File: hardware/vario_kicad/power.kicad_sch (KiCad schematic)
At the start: 17 parts, among them Q1 NMOS, Q2 PMOS

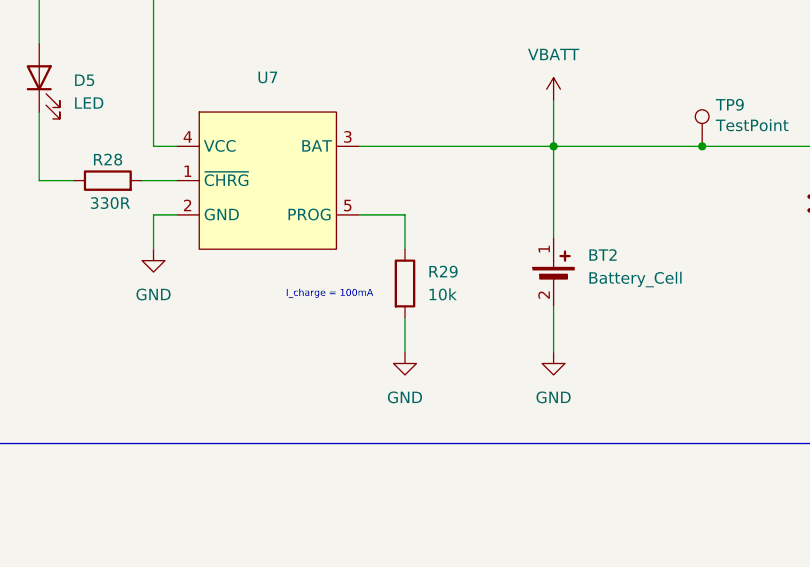
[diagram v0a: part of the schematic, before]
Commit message: update footprints, add LSE oscillator
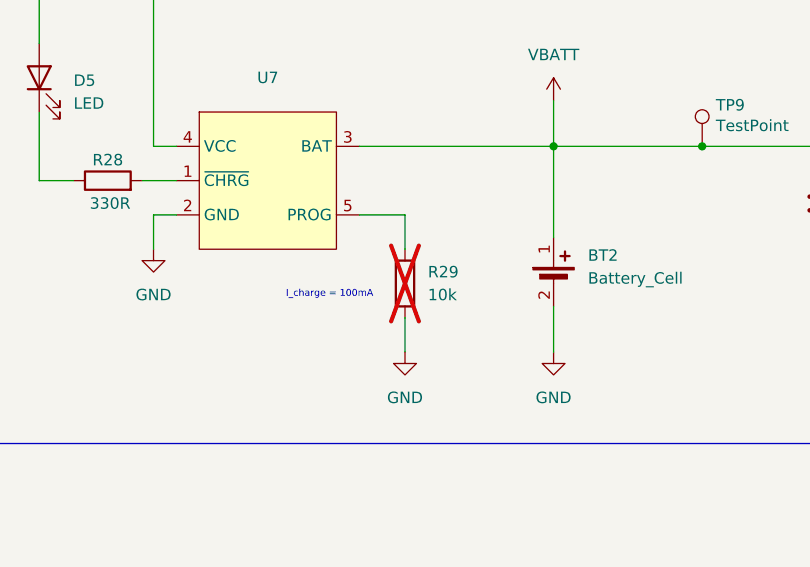
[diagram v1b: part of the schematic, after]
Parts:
- R22, R23, R24, R25, R28: footprint (none) -> Resistor_SMD:R_0402_1005Metric
- R29: footprint (none) -> Resistor_SMD:R_0402_1005Metric; now not fitted
- TP10, TP9: footprint (none) -> TestPoint:TestPoint_Pad_D1.0mm
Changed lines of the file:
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@@
 			)
 		)
-		(property "Footprint" ""
+		(property "Footprint" "Resistor_SMD:R_0402_1005Metric"
 			(at 54.102 158.75 90)
 			(effects
@@
 			)
 		)
-		(property "Footprint" ""
+		(property "Footprint" "Resistor_SMD:R_0402_1005Metric"
 			(at 80.772 146.05 90)
 			(effects
@@
 			)
 		)
-		(property "Footprint" ""
+		(property "Footprint" "Resistor_SMD:R_0402_1005Metric"
 			(at 80.772 161.29 90)
 			(effects
@@
 			)
 		)
-		(property "Footprint" ""
+		(property "Footprint" "Resistor_SMD:R_0402_1005Metric"
 			(at 57.15 58.928 90)
 			(effects
@@
 			)
 		)
-		(property "Footprint" ""
+		(property "Footprint" "TestPoint:TestPoint_Pad_D1.0mm"
 			(at 196.85 53.34 0)
 			(effects
@@
 			)
 		)
-		(property "Footprint" ""
+		(property "Footprint" "Resistor_SMD:R_0402_1005Metric"
 			(at 54.61 127.508 90)
 			(effects
@@
 			)
 		)
-		(property "Footprint" ""
+		(property "Footprint" "TestPoint:TestPoint_Pad_D1.0mm"
 			(at 128.27 53.34 0)
 			(effects
@@
 		(in_bom yes)
 		(on_board yes)
-		(dnp no)
+		(dnp yes)
 		(fields_autoplaced yes)
 		(property "Reference" "R29"
@@
 			)
 		)
-		(property "Footprint" ""
+		(property "Footprint" "Resistor_SMD:R_0402_1005Metric"
 			(at 88.392 68.58 90)
 			(effects

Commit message: start layout
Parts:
- added P1: USB_C_Plug_USB2.0, symbol_lib:my_usbc, symbol Connector:USB_C_Plug_USB2.0
- added R4: 5k1, Resistor_SMD:R_0402_1005Metric, symbol Device:R
- Q1, Q2: footprint (none) -> Package_TO_SOT_SMD:SOT-23_Handsoldering
- R29: now fitted
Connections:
- net GND: now also Q1.2 (S), P1.A1 (GND), P1.A12 (GND), P1.B1 (GND), P1.B12 (GND), P1.S1 (SHIELD), R4.1; no longer Q1.3 (S)
- net VBATT: now also Q2.2 (S), U8.3 (VIN); no longer Q2.3 (S), U8.2 (VOUT)
- net VBATT_SW: now also Q2.3 (D); no longer Q2.1 (D)
- net V_BATT_SW_EN: now also Q1.1 (G); no longer Q1.2 (G)
- net V_USB: now also P1.A4 (VBUS), P1.A9 (VBUS), P1.B4 (VBUS), P1.B9 (VBUS)
- new net: P1.A5 (CC), R4.2
- new net: Q1.3 (D), Q2.1 (G), R22.1
- new net USB_D+: P1.A6 (D+)
- new net USB_D-: P1.A7 (D-)
- no-connect marks 0 -> 1
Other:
- moved on the sheet: BT2, C14, C18, C19, D5, R28, TP10, TP9, U7, U8

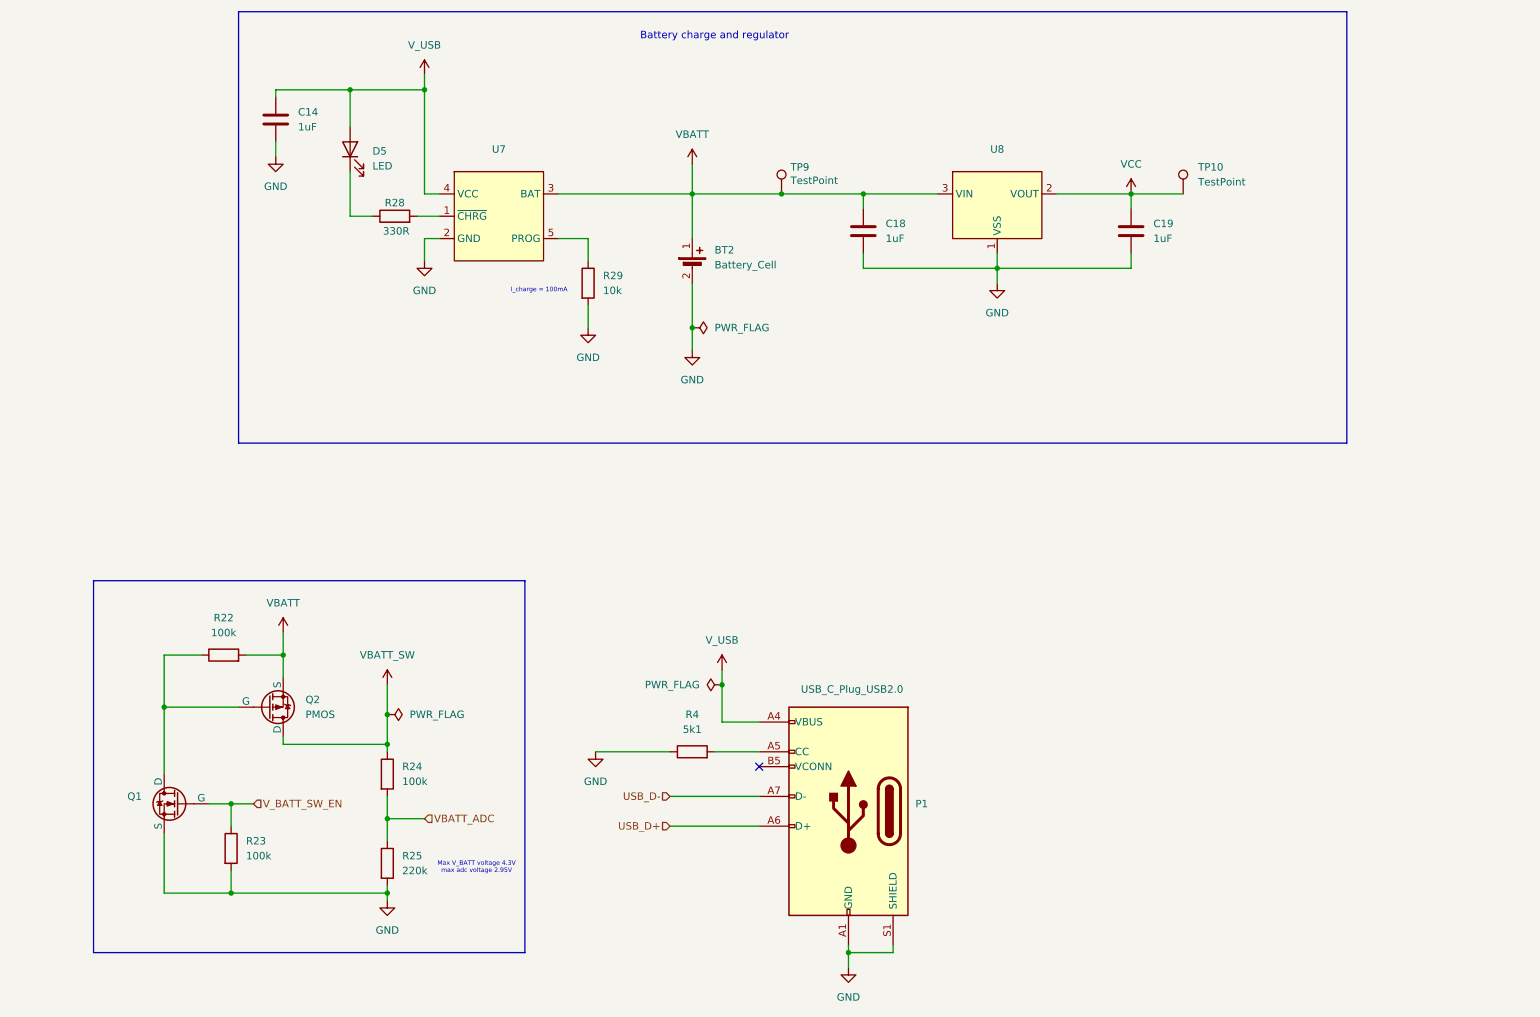
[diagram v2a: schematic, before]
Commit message: update usb c, minor other updates
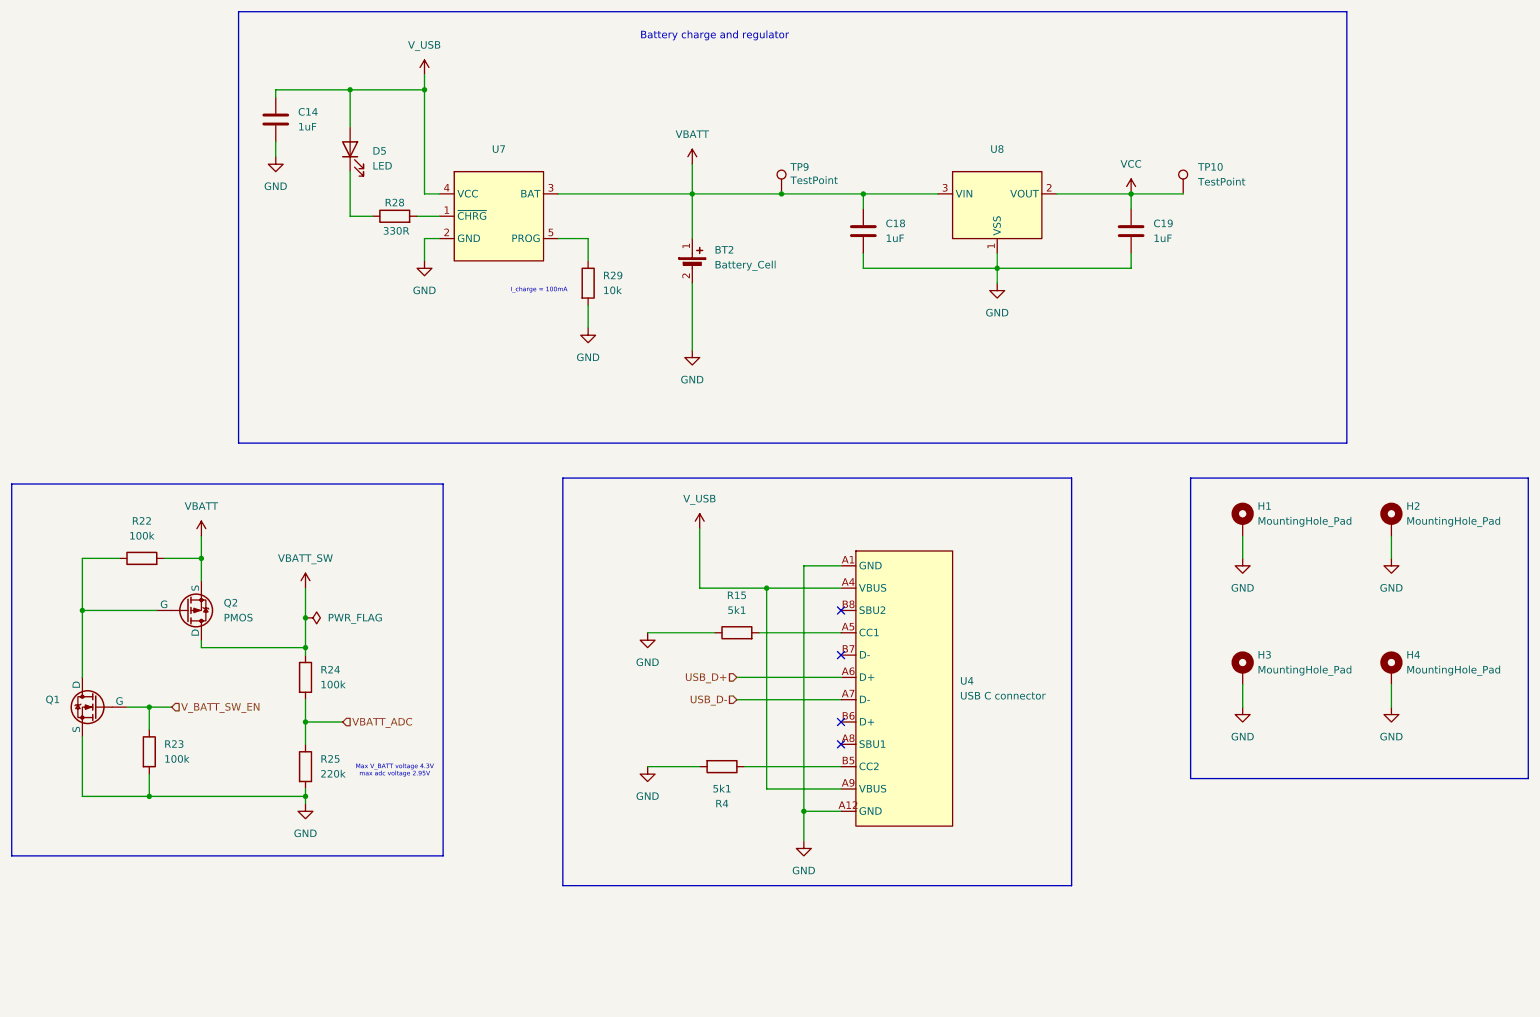
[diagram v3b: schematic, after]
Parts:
- removed P1: USB_C_Plug_USB2.0, symbol_lib:my_usbc, symbol Connector:USB_C_Plug_USB2.0
- added H1, H2, H3, H4: MountingHole_Pad, MountingHole:MountingHole_2.2mm_M2_ISO7380_Pad, symbol Mechanical:MountingHole_Pad
- added R15: 5k1, Resistor_SMD:R_0402_1005Metric, symbol Device:R
- added U4: USB C connector, symbol_lib:my_usbc, symbol New_Library:USB_C
- BT2: footprint symbol_lib:lipo_footprint -> symbol_lib:battery_th
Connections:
- net GND: now also R4.2, H1.1, H2.1, H3.1, H4.1, R15.1, U4.A1 (GND), U4.A12 (GND); no longer R4.1
- net USB_D+: now also U4.A6 (D+)
- net USB_D-: now also U4.A7 (D-)
- net V_USB: now also U4.A4 (VBUS), U4.A9 (VBUS)
- new net: R15.2, U4.A5 (CC1)
- new net: R4.1, U4.B5 (CC2)
- no-connect marks 1 -> 4
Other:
- moved on the sheet: Q1, Q2, R22, R23, R24, R25

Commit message: v1 review of power
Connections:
- net GND: now also U4.S1 (SHIELD)
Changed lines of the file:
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@@
 	)
 	(junction
+		(at 157.48 152.4)
+		(diameter 0)
+		(color 0 0 0 0)
+	)
+	(junction
 		(at 209.55 46.99)
 		(diameter 0)
@@
 	(wire
 		(pts
+			(xy 173.99 157.48) (xy 173.99 160.02)
+		)
+		(stroke
+			(width 0)
+			(type default)
+		)
+	)
+	(wire
+		(pts
 			(xy 163.83 46.99) (xy 163.83 49.53)
 		)
@@
 	(wire
 		(pts
+			(xy 173.99 160.02) (xy 157.48 160.02)
+		)
+		(stroke
+			(width 0)
+			(type default)
+		)
+	)
+	(wire
+		(pts
 			(xy 63.5 29.21) (xy 63.5 30.48)
 		)
@@
 	(wire
 		(pts
-			(xy 153.67 152.4) (xy 160.02 152.4)
+			(xy 153.67 152.4) (xy 157.48 152.4)
 		)
 		(stroke
@@
 	(wire
 		(pts
+			(xy 157.48 160.02) (xy 157.48 152.4)
+		)
+		(stroke
+			(width 0)
+			(type default)
+		)
+	)
+	(wire
+		(pts
 			(xy 76.2 29.21) (xy 88.9 29.21)
 		)
@@
 	(wire
 		(pts
+			(xy 157.48 152.4) (xy 160.02 152.4)
+		)
+		(stroke
+			(width 0)
+			(type default)
+		)
+	)
+	(wire
+		(pts
 			(xy 142.24 129.54) (xy 160.02 129.54)
 		)
@@
 			)
 		)
-		(property "Datasheet" "https://ngspice.sourceforge.io/docs/ngspice-html-manual/manual.xhtml#cha_MOSFETs"
+		(property "Datasheet" "https://www.lcsc.com/product-detail/MOSFETs_MDD-Microdiode-Semiconductor-AO3415_C840839.html"
 			(at 48.26 105.41 0)
 			(effects
@@
 		(pin "A7"
 		)
+		(pin "S1"
+		)
 		(instances

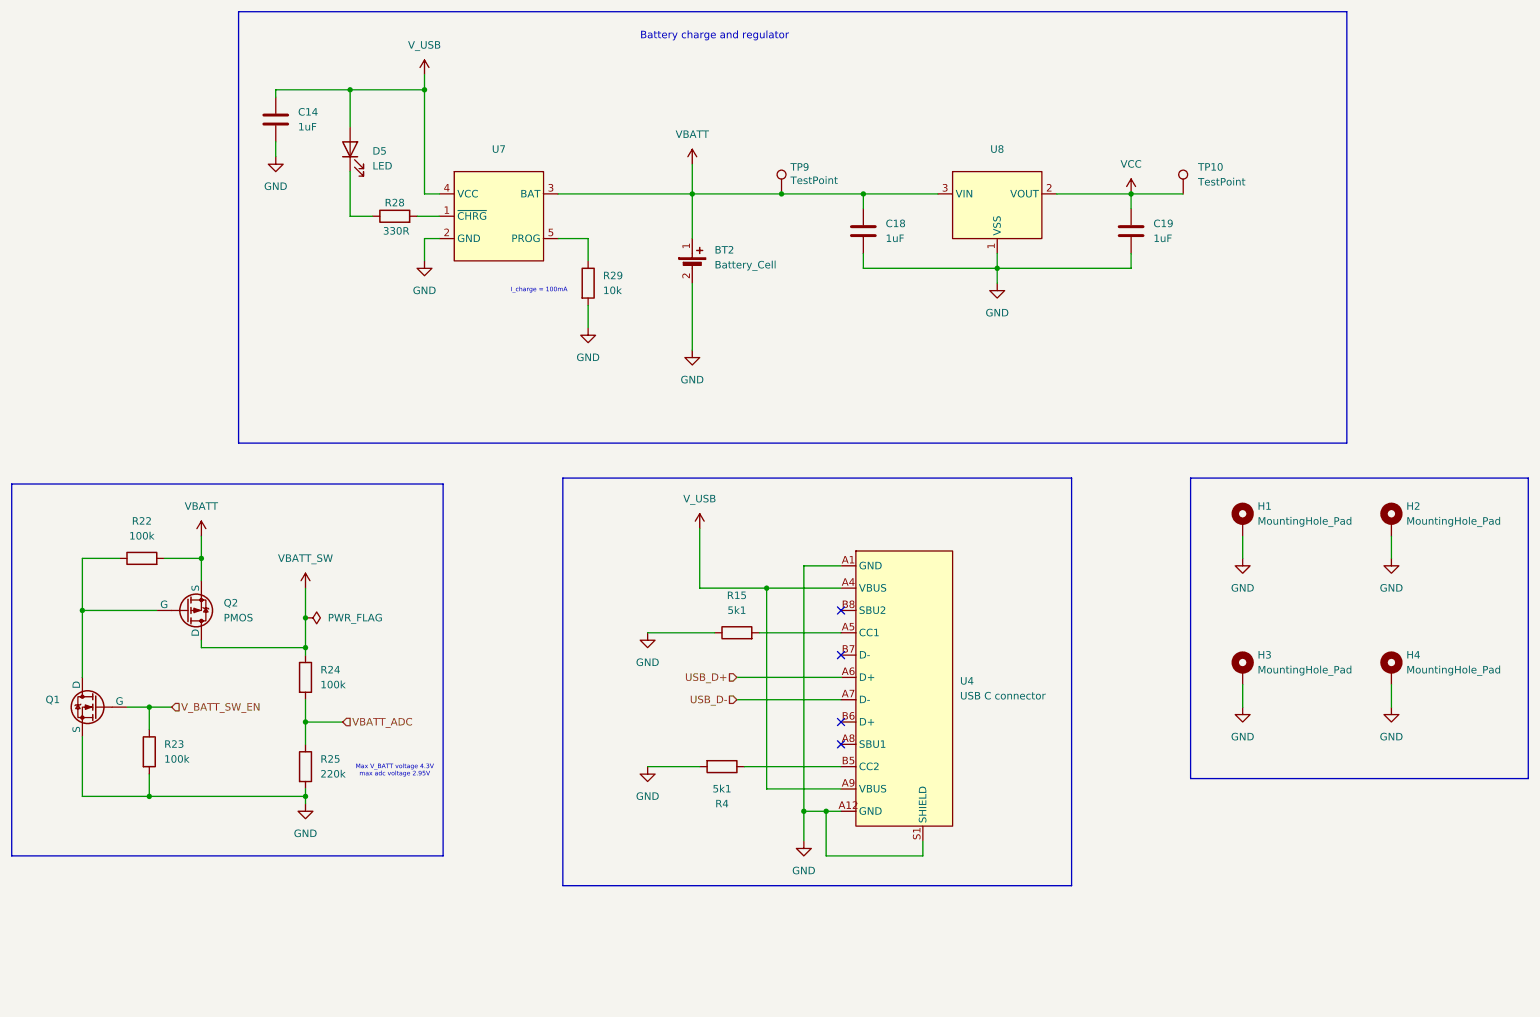
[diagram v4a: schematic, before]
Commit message: add optional current sense resistor
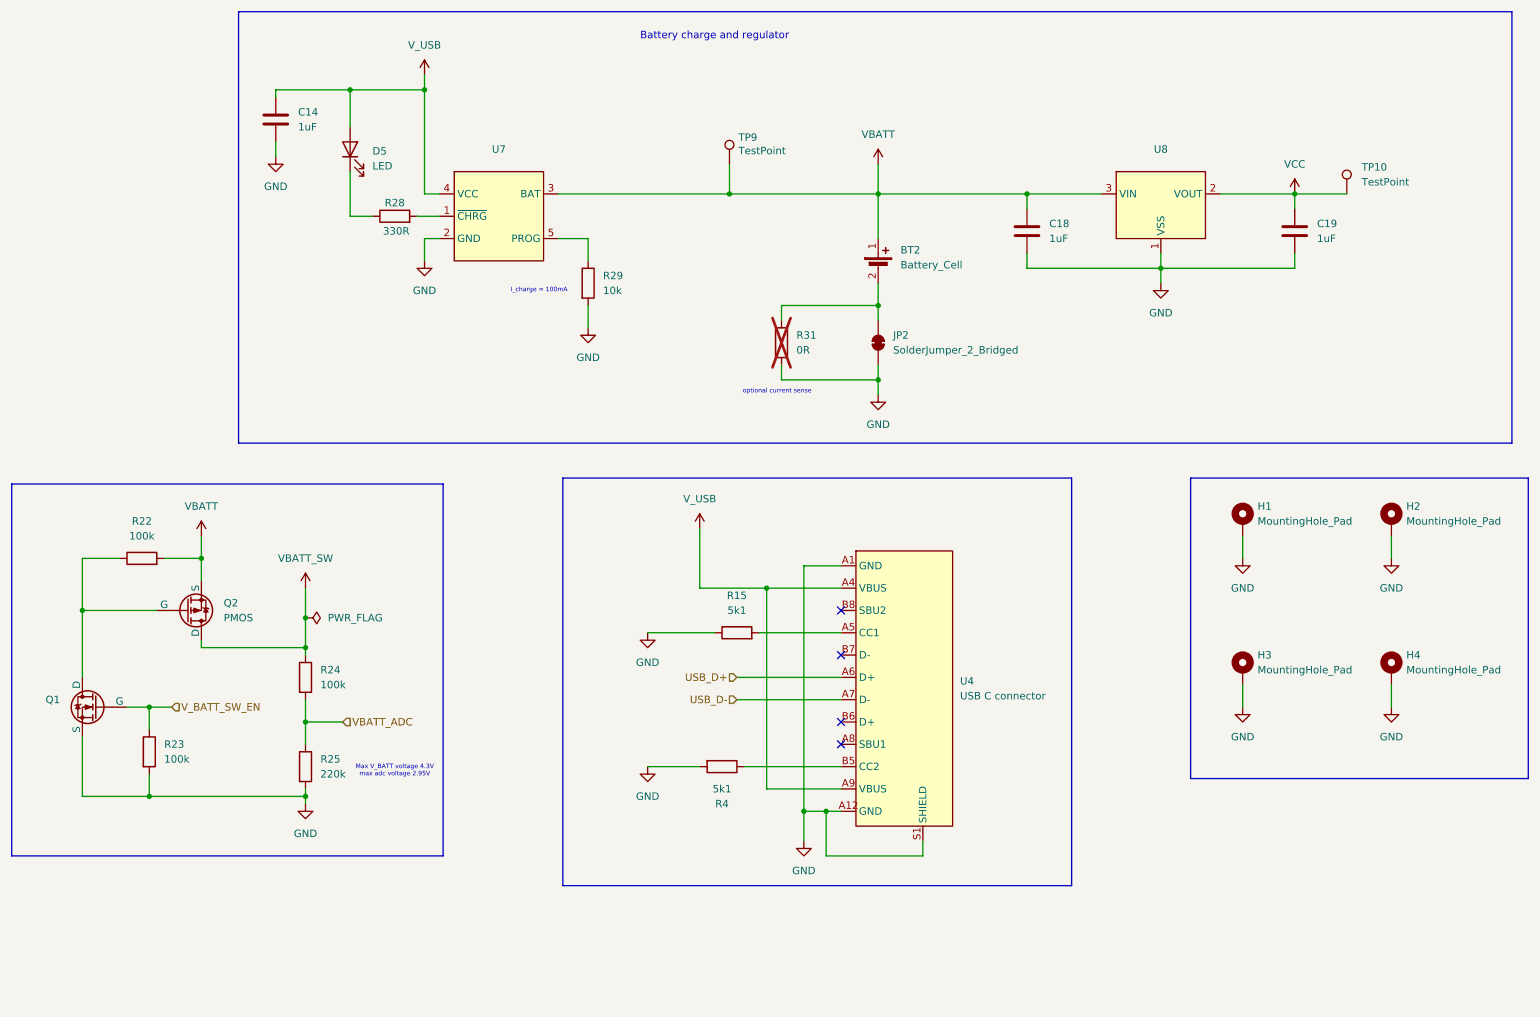
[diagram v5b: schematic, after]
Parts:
- added JP2: SolderJumper_2_Bridged, Jumper:SolderJumper-2_P1.3mm_Open_TrianglePad1.0x1.5mm, symbol Jumper:SolderJumper_2_Bridged
- added R31: 0R, symbol Device:R
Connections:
- net GND: now also JP2.1 (A), R31.2; no longer BT2.2 (-)
- new net: BT2.2 (-), JP2.2 (B), R31.1
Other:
- note added: "optional current sense"
- moved on the sheet: BT2, C18, C19, TP10, TP9, U8
